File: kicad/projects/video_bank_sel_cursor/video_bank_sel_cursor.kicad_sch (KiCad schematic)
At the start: 44 parts, among them J1 peripheral_addr_bus_connector, J2 peripheral_aux_connector, J3 peripheral_membank_connector, J4 Conn_01x16_Socket, J5 Conn_01x16_Socket, J6 video_aux, J7 Conn_01x16_Socket, J8 Conn_01x06_Socket, U1 74HC245, U10 74HC10, U11 74HC377, U12 74HC377, U14 74HC245, U15 74HC245, U2 74HC245, U3 74HC245, U4 74HC245, U5 74HC245, U6 74HC245, U7 74HC245, U8 74HC245, U9 74HC10

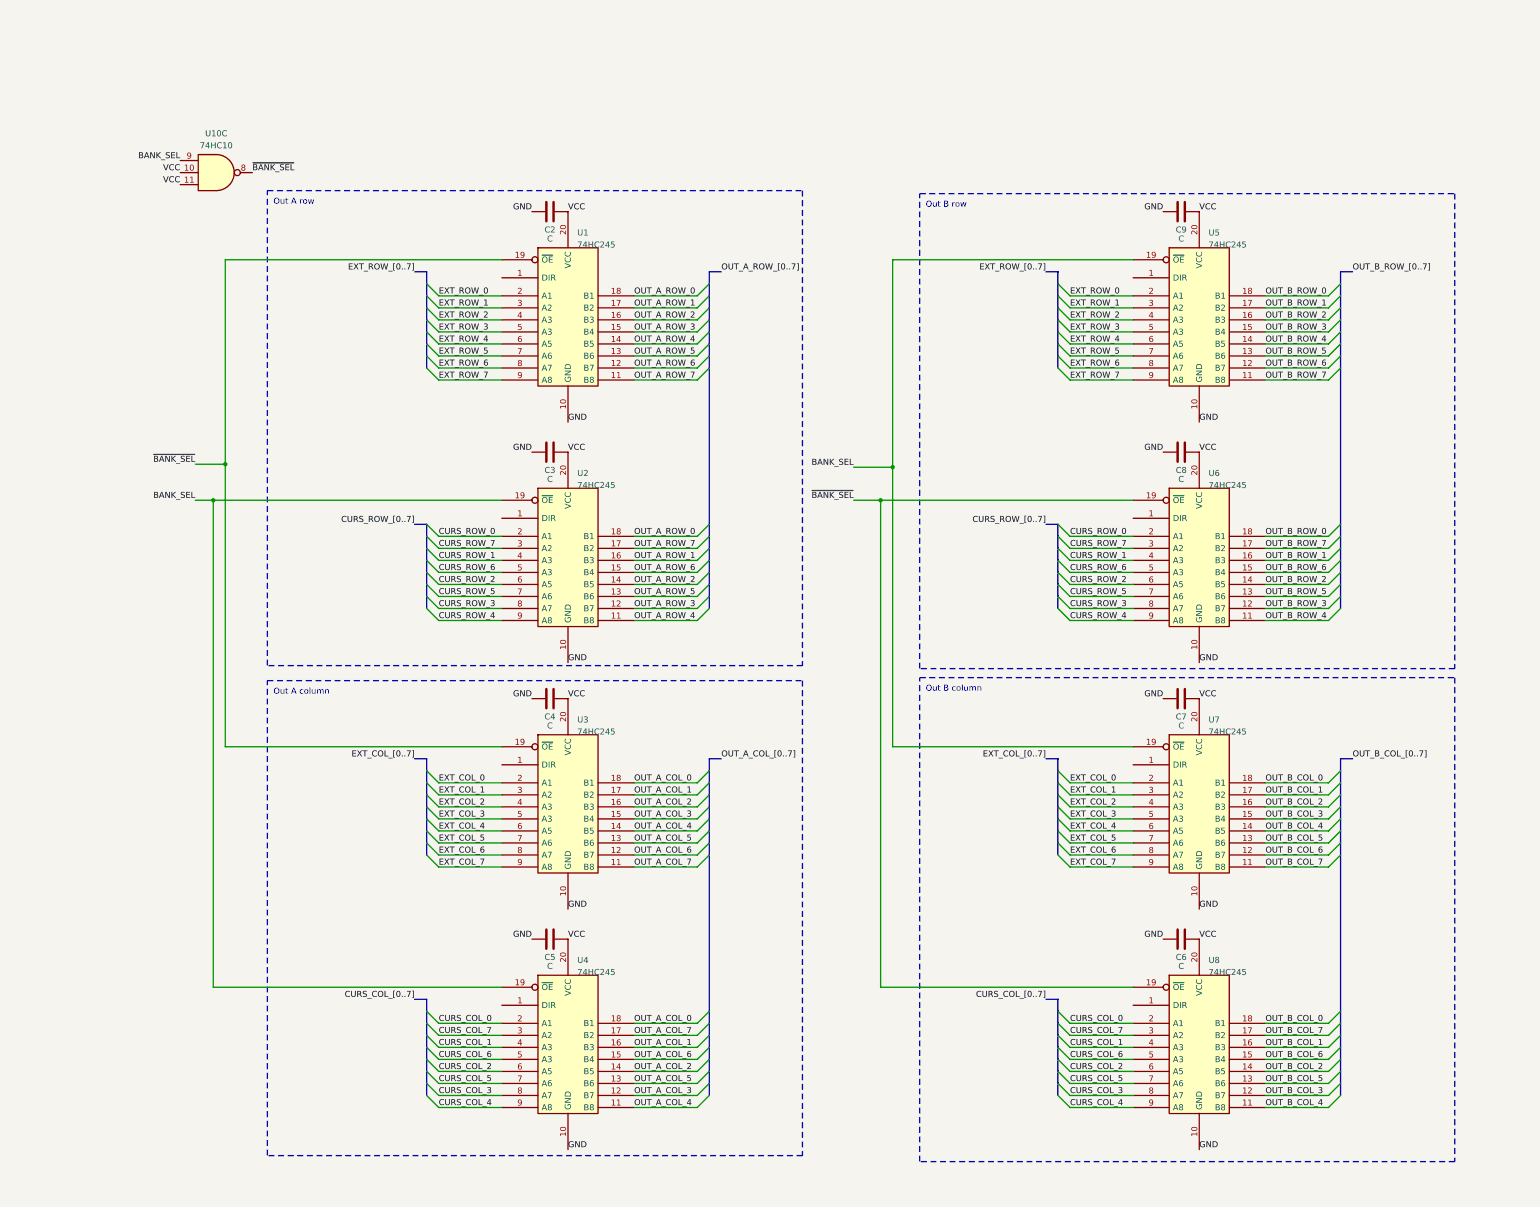
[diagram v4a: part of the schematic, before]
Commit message: Add indicator LEDs to shift status delay board. Bit of work on bank sel PCB.
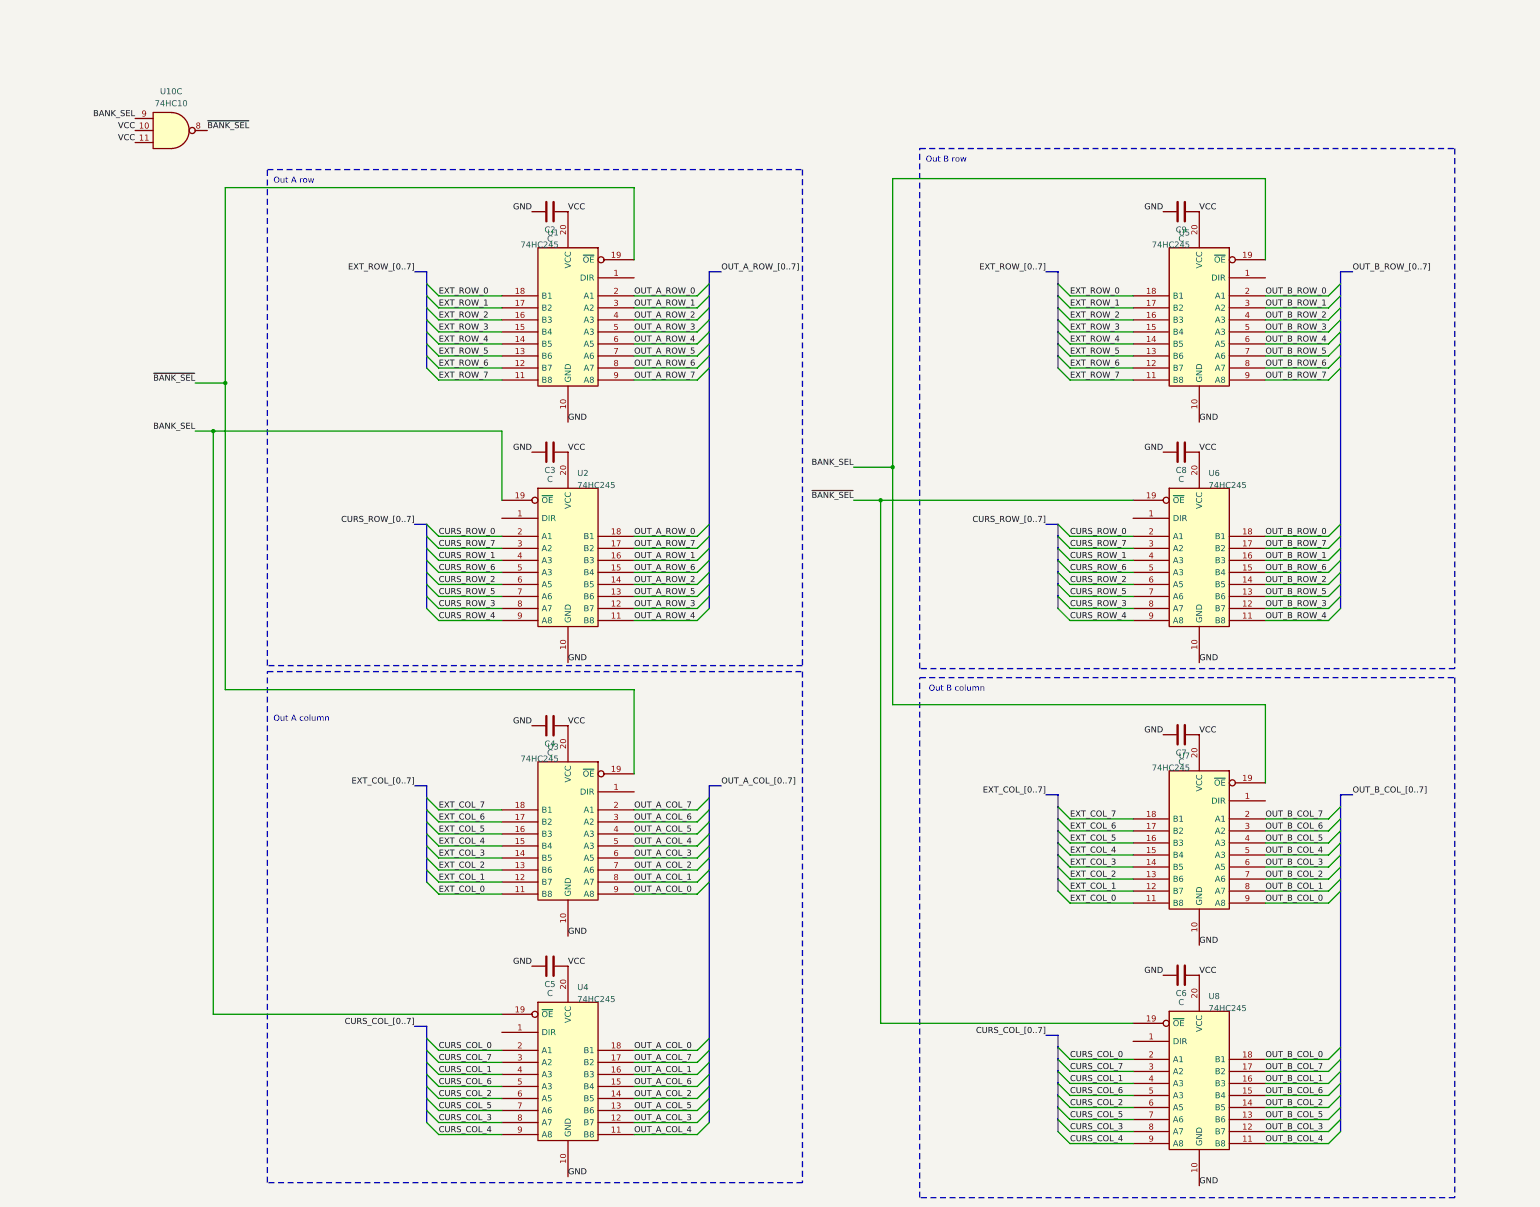
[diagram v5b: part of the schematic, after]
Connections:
- net EXT_COL_0: now also U3.11 (B8), U7.11 (B8); no longer U3.2 (A1), U7.2 (A1)
- net EXT_COL_1: now also U3.12 (B7), U7.12 (B7); no longer U3.3 (A2), U7.3 (A2)
- net EXT_COL_2: now also U3.13 (B6), U7.13 (B6); no longer U3.4 (A3), U7.4 (A3)
- net EXT_COL_3: now also U3.14 (B5), U7.14 (B5); no longer U3.5 (A3), U7.5 (A3)
- net EXT_COL_4: now also U3.15 (B4), U7.15 (B4); no longer U3.6 (A5), U7.6 (A5)
- net EXT_COL_5: now also U3.16 (B3), U7.16 (B3); no longer U3.7 (A6), U7.7 (A6)
- net EXT_COL_6: now also U3.17 (B2), U7.17 (B2); no longer U3.8 (A7), U7.8 (A7)
- net EXT_COL_7: now also U3.18 (B1), U7.18 (B1); no longer U3.9 (A8), U7.9 (A8)
- net EXT_ROW_0: now also U1.18 (B1), U5.18 (B1); no longer U1.2 (A1), U5.2 (A1)
- net EXT_ROW_1: now also U1.17 (B2), U5.17 (B2); no longer U1.3 (A2), U5.3 (A2)
- net EXT_ROW_2: now also U1.16 (B3), U5.16 (B3); no longer U1.4 (A3), U5.4 (A3)
- net EXT_ROW_3: now also U1.15 (B4), U5.15 (B4); no longer U1.5 (A3), U5.5 (A3)
- net EXT_ROW_4: now also U1.14 (B5), U5.14 (B5); no longer U1.6 (A5), U5.6 (A5)
- net EXT_ROW_5: now also U1.13 (B6), U5.13 (B6); no longer U1.7 (A6), U5.7 (A6)
- net EXT_ROW_6: now also U1.12 (B7), U5.12 (B7); no longer U1.8 (A7), U5.8 (A7)
- net EXT_ROW_7: now also U1.11 (B8), U5.11 (B8); no longer U1.9 (A8), U5.9 (A8)
- net OUT_A_COL_0: now also U3.9 (A8); no longer U3.18 (B1)
- net OUT_A_COL_1: now also U3.8 (A7); no longer U3.17 (B2)
- net OUT_A_COL_2: now also U3.7 (A6); no longer U3.16 (B3)
- net OUT_A_COL_3: now also U3.6 (A5); no longer U3.15 (B4)
- net OUT_A_COL_4: now also U3.5 (A3); no longer U3.14 (B5)
- net OUT_A_COL_5: now also U3.4 (A3); no longer U3.13 (B6)
- net OUT_A_COL_6: now also U3.3 (A2); no longer U3.12 (B7)
- net OUT_A_COL_7: now also U3.2 (A1); no longer U3.11 (B8)
- net OUT_A_ROW_0: now also U1.2 (A1); no longer U1.18 (B1)
- net OUT_A_ROW_1: now also U1.3 (A2); no longer U1.17 (B2)
- net OUT_A_ROW_2: now also U1.4 (A3); no longer U1.16 (B3)
- net OUT_A_ROW_3: now also U1.5 (A3); no longer U1.15 (B4)
- net OUT_A_ROW_4: now also U1.6 (A5); no longer U1.14 (B5)
- net OUT_A_ROW_5: now also U1.7 (A6); no longer U1.13 (B6)
- net OUT_A_ROW_6: now also U1.8 (A7); no longer U1.12 (B7)
- net OUT_A_ROW_7: now also U1.9 (A8); no longer U1.11 (B8)
- net OUT_B_COL_0: now also U7.9 (A8); no longer U7.18 (B1)
- net OUT_B_COL_1: now also U7.8 (A7); no longer U7.17 (B2)
- net OUT_B_COL_2: now also U7.7 (A6); no longer U7.16 (B3)
- net OUT_B_COL_3: now also U7.6 (A5); no longer U7.15 (B4)
- net OUT_B_COL_4: now also U7.5 (A3); no longer U7.14 (B5)
- net OUT_B_COL_5: now also U7.4 (A3); no longer U7.13 (B6)
- net OUT_B_COL_6: now also U7.3 (A2); no longer U7.12 (B7)
- net OUT_B_COL_7: now also U7.2 (A1); no longer U7.11 (B8)
- net OUT_B_ROW_0: now also U5.2 (A1); no longer U5.18 (B1)
- net OUT_B_ROW_1: now also U5.3 (A2); no longer U5.17 (B2)
- net OUT_B_ROW_2: now also U5.4 (A3); no longer U5.16 (B3)
- net OUT_B_ROW_3: now also U5.5 (A3); no longer U5.15 (B4)
- net OUT_B_ROW_4: now also U5.6 (A5); no longer U5.14 (B5)
- net OUT_B_ROW_5: now also U5.7 (A6); no longer U5.13 (B6)
- net OUT_B_ROW_6: now also U5.8 (A7); no longer U5.12 (B7)
- net OUT_B_ROW_7: now also U5.9 (A8); no longer U5.11 (B8)
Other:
- moved on the sheet: C4, C5, C6, C7, U10C, U3, U4, U7, U8

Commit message: First pass of video bank sel PCB complete.
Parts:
- removed C1: C, Capacitor_THT:C_Disc_D5.0mm_W2.5mm_P5.00mm, symbol Device:C
- removed R1: R_US, Resistor_THT:R_Axial_DIN0207_L6.3mm_D2.5mm_P10.16mm_Horizontal, symbol Device:R_US
- removed TP1: TestPoint, Connector_Pin:Pin_D1.0mm_L10.0mm, symbol Connector:TestPoint
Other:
- moved on the sheet: C10, C11, C12, C13, C14, C15, C2, C3, C4, C5, C6, C7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

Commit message: Row and column order made consistent on top connectors. Bank Sel cursor tech checked.
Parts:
- added R1, R4, R5: 10K, Resistor_THT:R_Axial_DIN0207_L6.3mm_D2.5mm_P10.16mm_Horizontal, symbol Device:R_US
- C97, C98, C99: value C_Polarized -> 33uF
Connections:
- net GND: now also U1.1 (DIR), U14.1 (DIR), U15.1 (DIR), U3.1 (DIR), U5.1 (DIR), U7.1 (DIR)
- net VCC: now also U2.1 (DIR), U4.1 (DIR), U6.1 (DIR), U8.1 (DIR), R1.2, R4.2, R5.2
- net ~{BANK_SEL}: now also R1.1
- net ~{CURSOR_COL_WTM}: now also R4.1
- net ~{CURSOR_ROW_WTM}: now also R5.1
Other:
- moved on the sheet: U10A, U9C
